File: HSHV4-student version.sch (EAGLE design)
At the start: 34 parts, among them IC1 DS3231, IC4 IO_EXPANDER, K1 PIN20X2, Q1 MOSFET-NCHANNEL2N7000, Q2 MOSFET-NCHANNEL2N7000, U1 256K_EEPROM

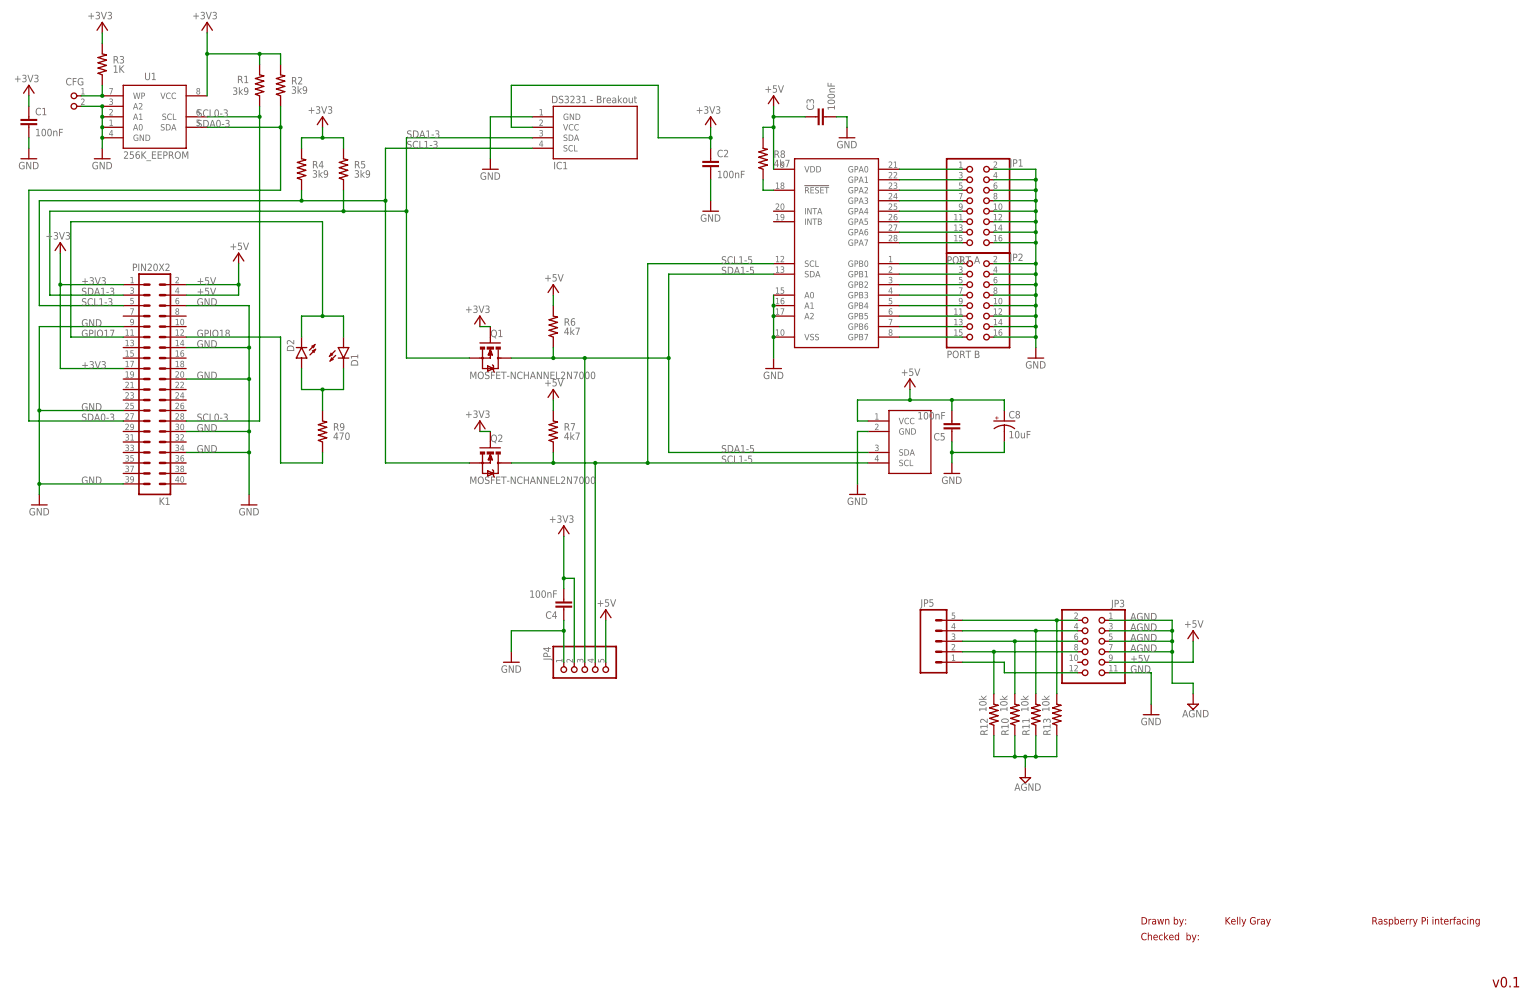
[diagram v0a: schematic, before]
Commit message: Made larger pads
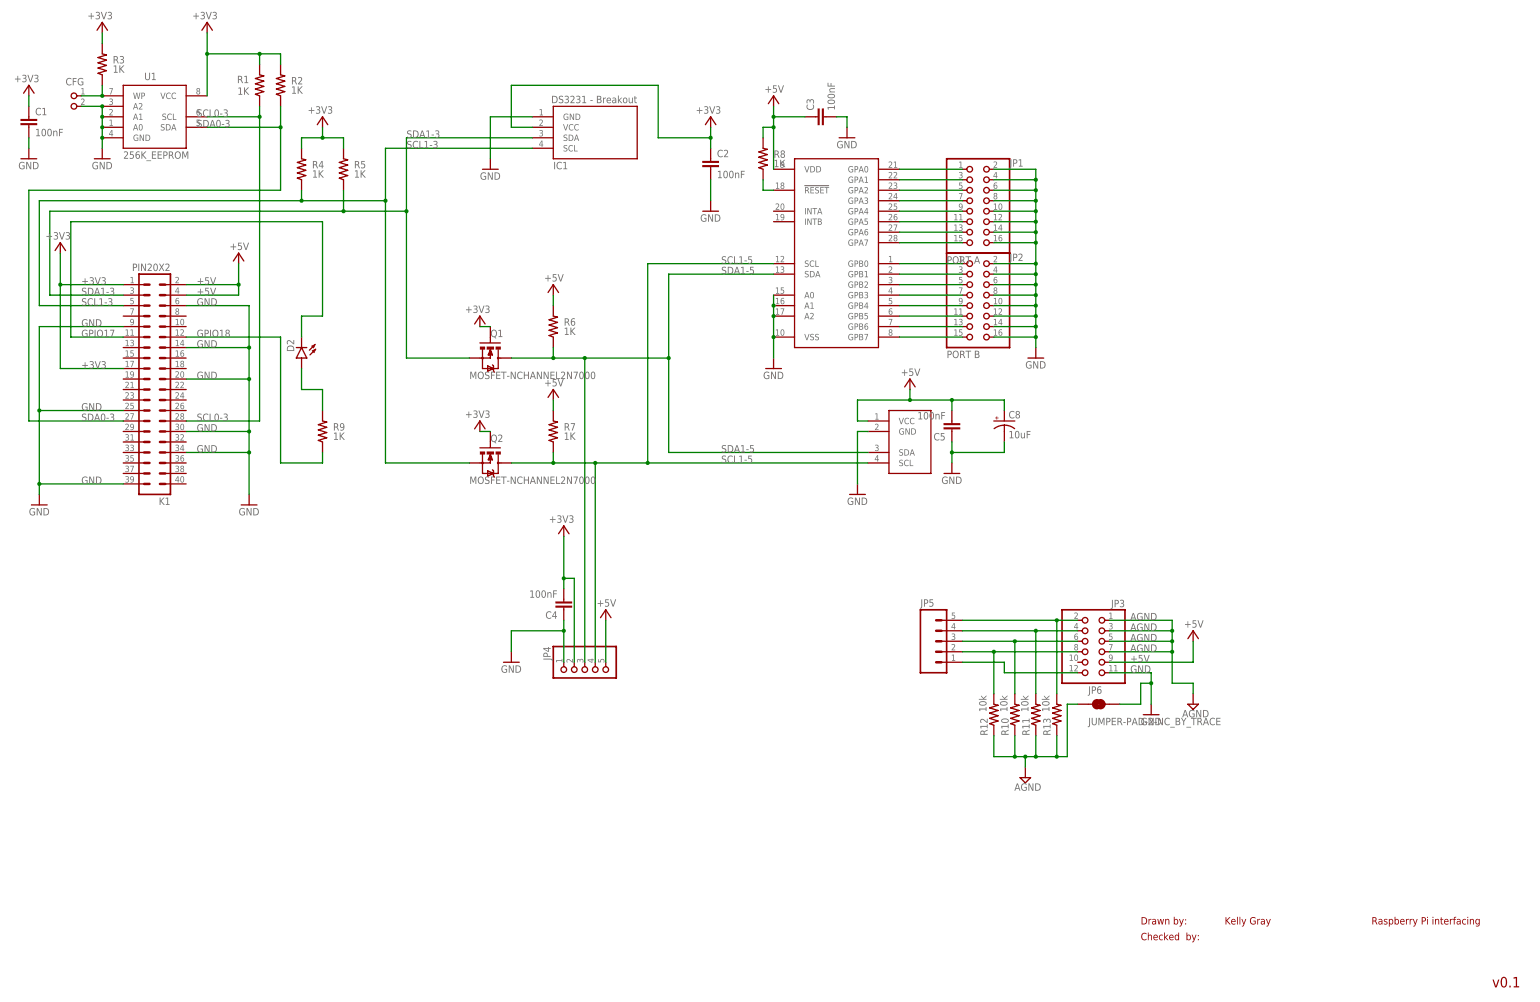
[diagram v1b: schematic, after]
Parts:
- removed D1: (no value), SparkFun-LED:LED-3MM-NO_SILK
- added JP6: JUMPER-PAD-2-NC_BY_TRACE, SparkFun-Passives:JUMPER-PAD-2-NC_BY_TRACE
- R1, R2, R4, R5: value 3k9 -> 1K
- R6, R7, R8: value 4k7 -> 1K
- R9: value 470 -> 1K
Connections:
- net AGND: now also JP6.1
- net GND: now also JP6.2
- net GPIO17: no longer D1.A
- net N$2: no longer D1.C
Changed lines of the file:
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@@
 <layer number="112" name="tSilk" color="7" fill="1" visible="no" active="yes"/>
 <layer number="113" name="ReferenceLS" color="7" fill="1" visible="no" active="no"/>
+<layer number="114" name="Badge_Outline" color="7" fill="1" visible="yes" active="yes"/>
+<layer number="115" name="ReferenceISLANDS" color="7" fill="1" visible="yes" active="yes"/>
 <layer number="116" name="Patch_BOT" color="7" fill="1" visible="yes" active="yes"/>
 <layer number="118" name="Rect_Pads" color="7" fill="1" visible="no" active="no"/>
@@
 <class number="0" name="default" width="0" drill="0">
 </class>
+<class number="1" name="TopSide" width="0" drill="0">
+</class>
 </classes>
 <parts>
@@
 <part name="U1" library="SenseHat" deviceset="256K_EEPROM" device=""/>
 <part name="GND10" library="supply1" deviceset="GND" device=""/>
-<part name="R1" library="SparkFun-Resistors" deviceset="1KOHM-1/4W-1%(PTH)" device="" value="3k9">
+<part name="R1" library="SparkFun-Resistors" deviceset="1KOHM-1/4W-1%(PTH)" device="" value="1K">
 <attribute name="TOLERANCE" value="5%"/>
 </part>
@@
 <attribute name="DIELECTRIC" value="X7R"/>
 </part>
-<part name="R2" library="SparkFun-Resistors" deviceset="1KOHM-1/4W-1%(PTH)" device="" value="3k9">
+<part name="R2" library="SparkFun-Resistors" deviceset="1KOHM-1/4W-1%(PTH)" device="" value="1K">
 <attribute name="TOLERANCE" value="5%"/>
 </part>
@@
 <part name="JP5" library="SparkFun-Connectors" deviceset="M05" device="PTH"/>
 <part name="U$1" library="SenseHat" deviceset="PCF8591" device=""/>
-<part name="R4" library="SparkFun-Resistors" deviceset="1KOHM-1/4W-1%(PTH)" device="" value="3k9">
-<attribute name="TOLERANCE" value="5%"/>
-</part>
-<part name="R5" library="SparkFun-Resistors" deviceset="1KOHM-1/4W-1%(PTH)" device="" value="3k9">
-<attribute name="TOLERANCE" value="5%"/>
-</part>
-<part name="R9" library="SparkFun-Resistors" deviceset="1KOHM-1/4W-1%(PTH)" device="" value="470">
-<attribute name="TOLERANCE" value="5%"/>
-</part>
-<part name="R6" library="SparkFun-Resistors" deviceset="1KOHM-1/4W-1%(PTH)" device="" value="4k7">
-<attribute name="TOLERANCE" value="5%"/>
-</part>
-<part name="R7" library="SparkFun-Resistors" deviceset="1KOHM-1/4W-1%(PTH)" device="" value="4k7">
-<attribute name="TOLERANCE" value="5%"/>
-</part>
-<part name="D1" library="SparkFun-LED" deviceset="LED" device="-3MM-NO_SILK"/>
+<part name="R4" library="SparkFun-Resistors" deviceset="1KOHM-1/4W-1%(PTH)" device="" value="1K">
+<attribute name="TOLERANCE" value="5%"/>
+</part>
+<part name="R5" library="SparkFun-Resistors" deviceset="1KOHM-1/4W-1%(PTH)" device="" value="1K">
+<attribute name="TOLERANCE" value="5%"/>
+</part>
+<part name="R9" library="SparkFun-Resistors" deviceset="1KOHM-1/4W-1%(PTH)" device="" value="1K">
+<attribute name="TOLERANCE" value="5%"/>
+</part>
+<part name="R6" library="SparkFun-Resistors" deviceset="1KOHM-1/4W-1%(PTH)" device="" value="1K">
+<attribute name="TOLERANCE" value="5%"/>
+</part>
+<part name="R7" library="SparkFun-Resistors" deviceset="1KOHM-1/4W-1%(PTH)" device="" value="1K">
+<attribute name="TOLERANCE" value="5%"/>
+</part>
 <part name="D2" library="SparkFun-LED" deviceset="LED" device="-3MM-NO_SILK"/>
 <part name="C2" library="SparkFun-Capacitors" deviceset="0.1UF-50V-20%(PTH)" device="KIT-EZ" value="100nF">
@@
 <attribute name="DIELECTRIC" value="X7R"/>
 </part>
-<part name="R8" library="SparkFun-Resistors" deviceset="1KOHM-1/4W-1%(PTH)" device="" value="4k7">
+<part name="R8" library="SparkFun-Resistors" deviceset="1KOHM-1/4W-1%(PTH)" device="" value="1K">
 <attribute name="TOLERANCE" value="5%"/>
 </part>
@@
 <attribute name="TOLERANCE" value="5%"/>
 </part>
+<part name="JP6" library="SparkFun-Passives" deviceset="JUMPER-PAD-2-NC_BY_TRACE" device=""/>
 </parts>
 <sheets>
@@
 <attribute name="VALUE" x="149.86" y="137.668" size="1.778" layer="96"/>
 </instance>
-<instance part="D1" gate="G$1" x="96.52" y="160.02"/>
 <instance part="D2" gate="G$1" x="86.36" y="157.48" rot="R180"/>
 <instance part="C2" gate="G$1" x="185.42" y="203.2">
@@
 <attribute name="VALUE" x="267.462" y="71.755" size="1.778" layer="96" rot="R90"/>
 </instance>
+<instance part="JP6" gate="G$1" x="279.4" y="73.66"/>
 </instances>
 <busses>
@@
 <segment>
 <pinref part="GND13" gate="1" pin="GND"/>
-<wire x1="292.1" y1="81.28" x2="292.1" y2="73.66" width="0.1524" layer="91"/>
+<wire x1="292.1" y1="81.28" x2="292.1" y2="78.74" width="0.1524" layer="91"/>
 <label x="287.02" y="81.28" size="1.778" layer="95"/>
 <pinref part="JP3" gate="A" pin="11"/>
+<wire x1="292.1" y1="78.74" x2="292.1" y2="73.66" width="0.1524" layer="91"/>
 <wire x1="292.1" y1="81.28" x2="281.94" y2="81.28" width="0.1524" layer="91"/>
+<pinref part="JP6" gate="G$1" pin="2"/>
+<wire x1="284.48" y1="73.66" x2="289.56" y2="73.66" width="0.1524" layer="91"/>
+<wire x1="289.56" y1="73.66" x2="289.56" y2="78.74" width="0.1524" layer="91"/>
+<wire x1="289.56" y1="78.74" x2="292.1" y2="78.74" width="0.1524" layer="91"/>
+<junction x="292.1" y="78.74"/>
 </segment>
 <segment>
@@
 <wire x1="246.38" y1="93.98" x2="269.24" y2="93.98" width="0.1524" layer="91"/>
 <wire x1="269.24" y1="93.98" x2="274.32" y2="93.98" width="0.1524" layer="91"/>
-<wire x1="269.24" y1="76.2" x2="269.24" y2="93.98" width="0.1524" layer="91"/>
 <junction x="269.24" y="93.98"/>
 <pinref part="JP5" gate="G$1" pin="5"/>
 <pinref part="R13" gate="G$1" pin="2"/>
+<wire x1="269.24" y1="76.2" x2="269.24" y2="93.98" width="0.1524" layer="91"/>
 </segment>
 </net>
@@
 <pinref part="R11" gate="G$1" pin="1"/>
 <pinref part="R13" gate="G$1" pin="1"/>
+<pinref part="JP6" gate="G$1" pin="1"/>
+<wire x1="274.32" y1="73.66" x2="271.78" y2="73.66" width="0.1524" layer="91"/>
+<wire x1="271.78" y1="73.66" x2="271.78" y2="60.96" width="0.1524" layer="91"/>
+<wire x1="271.78" y1="60.96" x2="269.24" y2="60.96" width="0.1524" layer="91"/>
+<junction x="269.24" y="60.96"/>
 </segment>
 </net>
@@
 <wire x1="86.36" y1="154.94" x2="86.36" y2="149.86" width="0.1524" layer="91"/>
 <wire x1="86.36" y1="149.86" x2="91.44" y2="149.86" width="0.1524" layer="91"/>
-<wire x1="91.44" y1="149.86" x2="96.52" y2="149.86" width="0.1524" layer="91"/>
-<wire x1="96.52" y1="149.86" x2="96.52" y2="154.94" width="0.1524" layer="91"/>
 <wire x1="91.44" y1="144.78" x2="91.44" y2="149.86" width="0.1524" layer="91"/>
-<junction x="91.44" y="149.86"/>
 <pinref part="R9" gate="G$1" pin="2"/>
-<pinref part="D1" gate="G$1" pin="C"/>
 <pinref part="D2" gate="G$1" pin="A"/>
 </segment>
@@
 <net name="GPIO17" class="0">
 <segment>
-<wire x1="96.52" y1="162.56" x2="96.52" y2="167.64" width="0.1524" layer="91"/>
-<wire x1="96.52" y1="167.64" x2="91.44" y2="167.64" width="0.1524" layer="91"/>
 <wire x1="91.44" y1="167.64" x2="86.36" y2="167.64" width="0.1524" layer="91"/>
 <wire x1="86.36" y1="167.64" x2="86.36" y2="162.56" width="0.1524" layer="91"/>
@@
 <wire x1="30.48" y1="190.5" x2="91.44" y2="190.5" width="0.1524" layer="91"/>
 <wire x1="91.44" y1="190.5" x2="91.44" y2="167.64" width="0.1524" layer="91"/>
-<junction x="91.44" y="167.64"/>
 <label x="33.02" y="162.56" size="1.778" layer="95"/>
-<pinref part="D1" gate="G$1" pin="A"/>
 <pinref part="D2" gate="G$1" pin="C"/>
 </segment>
